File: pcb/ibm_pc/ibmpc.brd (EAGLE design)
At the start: 56 x 65 mm, 47 parts, among them IC1 STM32F072C8T6, SW1 324_SW, SW2 324_SW, U1 MAX3232

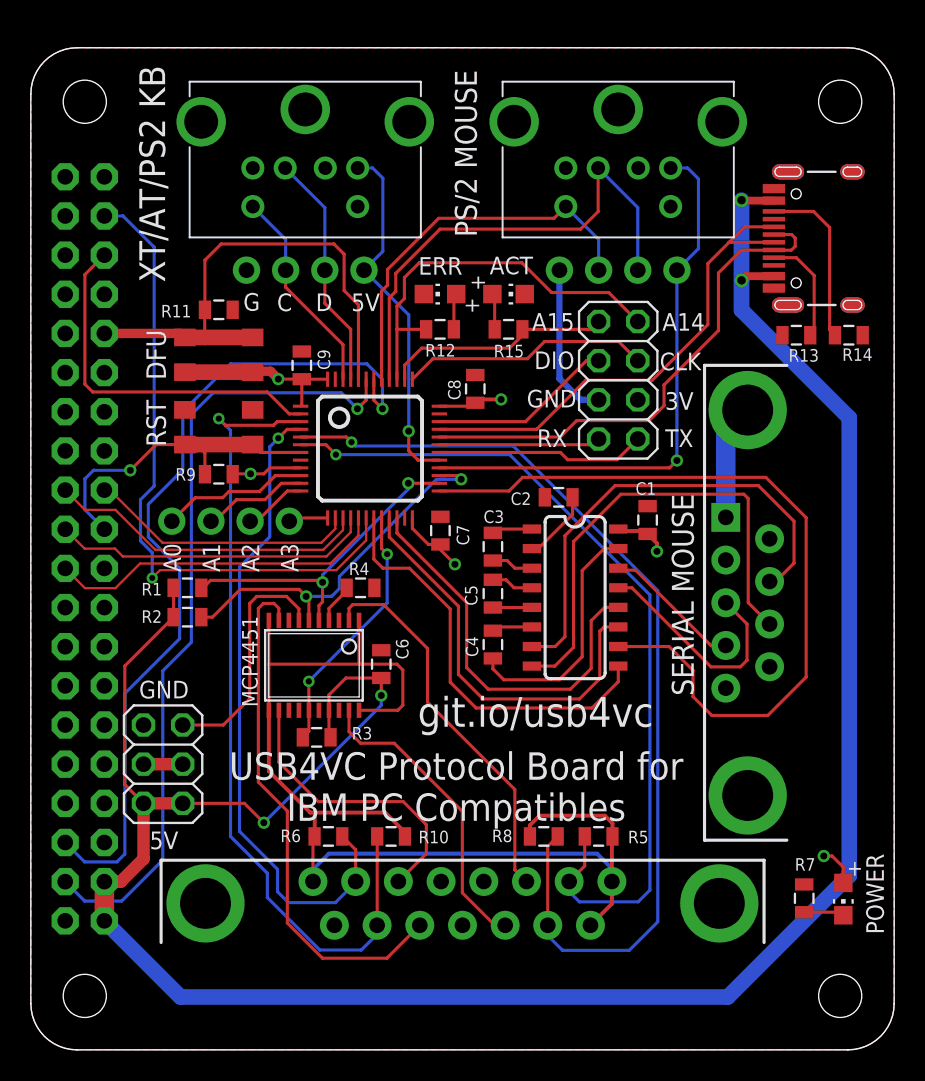
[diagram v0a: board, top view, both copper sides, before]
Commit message: added resistor to digipot
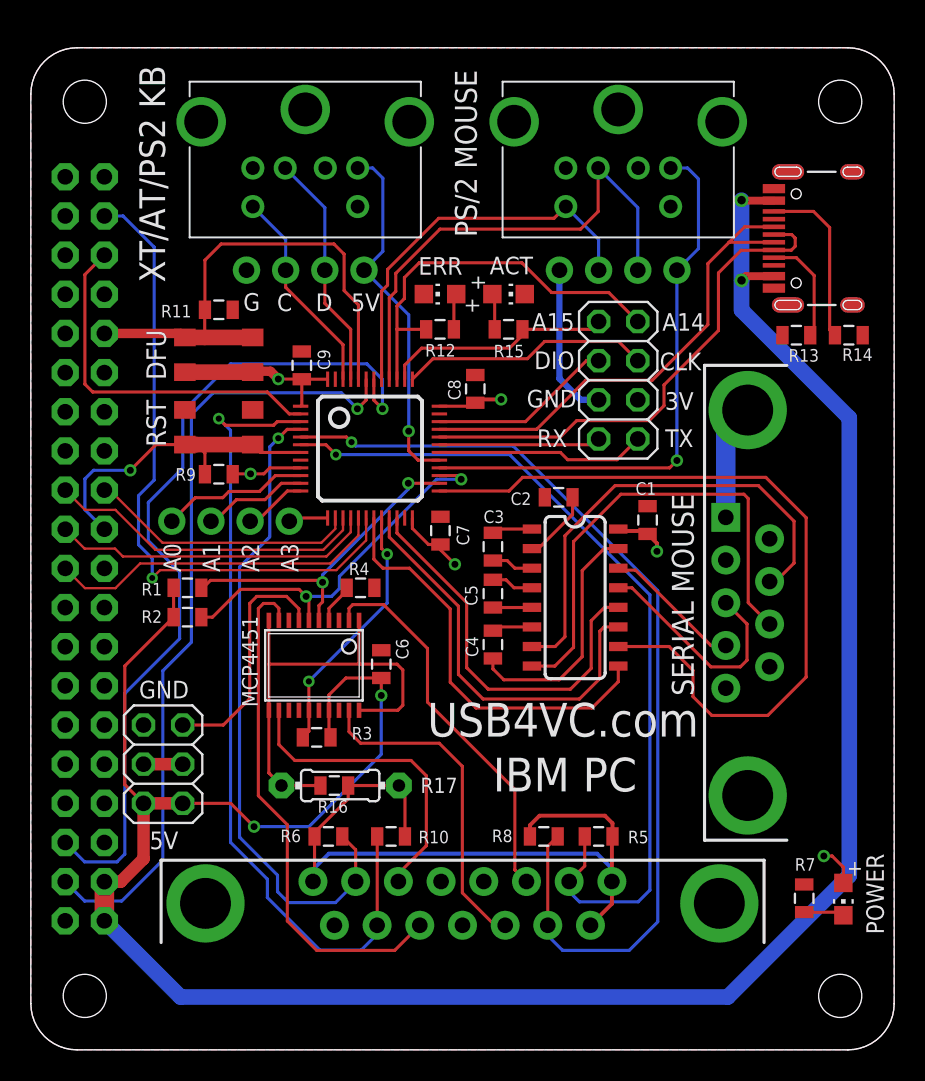
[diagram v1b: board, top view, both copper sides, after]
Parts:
- added R16: 100, SparkFun-Passives:0805
- added R17: (no value), adafruit:0204/7
- R12, R15, R7: value 2K -> 5.1K
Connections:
- new net N$17: R16.2, R17.1, U$5.1, U$5.10, U$5.11, U$5.20
- net +UB: now also R16.1, R17.2; no longer U$5.1, U$5.10, U$5.11, U$5.20
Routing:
- net N$17: track 0.00 -> 30.6 mm
- net +UB: track 77.6 -> 49.5 mm
- net +5V: track 157.3 -> 159.3 mm
- net X2_W2: track 19.8 -> 21.5 mm
- net Y1_W0: track 19.0 -> 20.2 mm
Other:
- board text added: "IBM PC"
- board text added: "USB4VC Protocol Card for IBM PC Compatible"
- board text added: "USB4VC.com"
- board text removed: "USB4VC Protocol Board for IBM PC Compatibles"
- board text removed: "git.io/usb4vc"

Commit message: updated IBM PC card
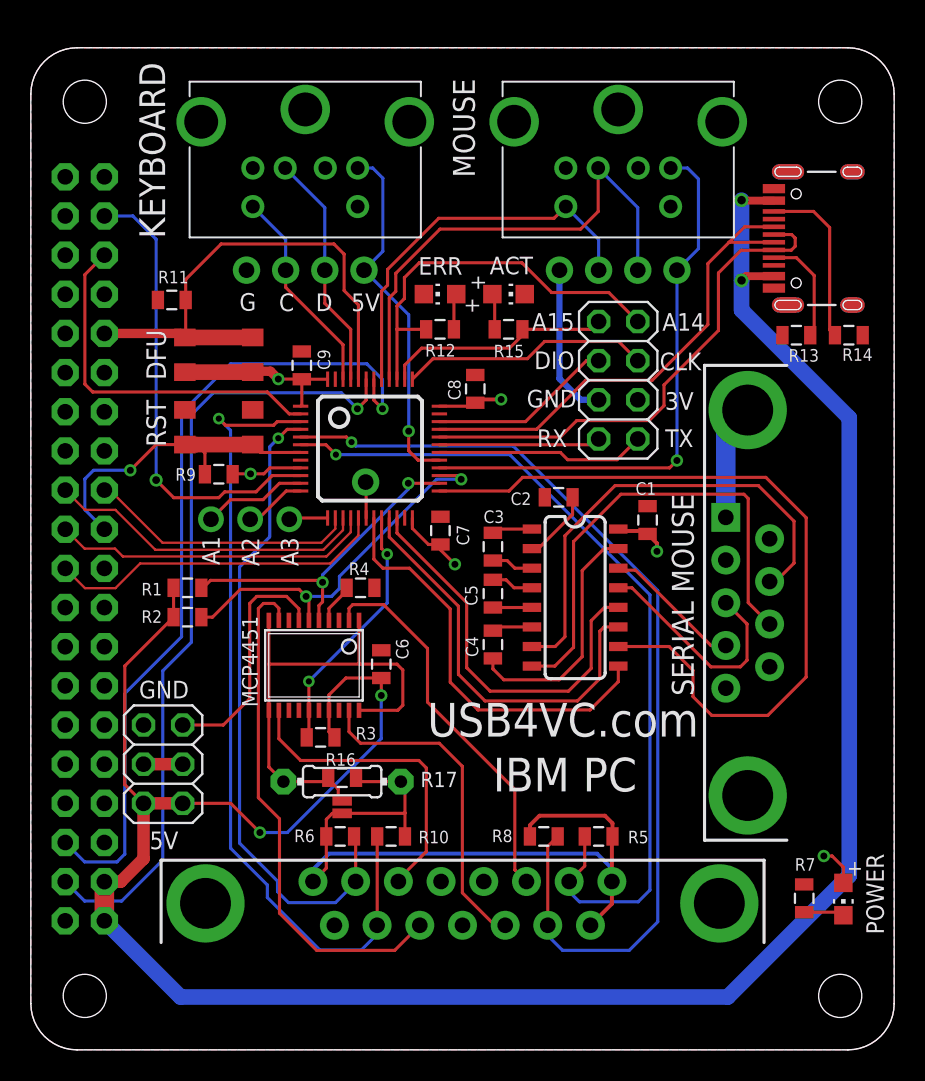
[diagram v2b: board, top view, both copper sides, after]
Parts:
- removed U$10: PINHD1X4, adafruit_changed:1X04-CLEANBIG
- added JP4: (no value), adafruit:1X03-CLEANBIG
- added JP5: JUMPER-SMT_2_NO_NO-SILK, SparkFun-Jumpers:SMT-JUMPER_2_NO_NO-SILK
- added JP6: (no value), adafruit:1X01-CLEANBIG
- moved R11 3.11 mm to (9.14, 48.6), turned to 0 degrees
- moved R6 0.76 mm to (20.1, 13.8)
- moved R16 0.72 mm to (20.2, 17.7)
- moved R17 0.28 mm to (20.2, 17.4)
- moved R3 0.25 mm to (18.8, 20.3)
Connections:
- removed net N$38: IC1.10, U$10.1
- new net N$30: IC1.18, JP6.1
- net +UB: now also JP5.2
- net N$17: now also JP5.1
- net N$3: now also IC1.10; no longer IC1.18
- net N$39: now also JP4.3; no longer U$10.2
- net N$40: now also JP4.2; no longer U$10.3
- net N$41: now also JP4.1; no longer U$10.4
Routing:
- net N$3: track 42.7 -> 30.0 mm
- net N$38: track 9.58 -> 0.00 mm
- net +UB: track 49.5 -> 51.9 mm
- net N$30: track 0.00 -> 2.34 mm
- net N$17: track 30.6 -> 32.7 mm
- net N$22: track 55.3 -> 53.6 mm
- net N$18: track 33.0 -> 33.5 mm
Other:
- board text added: "B0"
- board text added: "KEYBOARD"
- board text added: "MOUSE"
- board text added: "USB4VC Protocol Card for IBM PC Compatibles"
- board text removed: "A0"
- board text removed: "PS/2 MOUSE"
- board text removed: "USB4VC Protocol Card for IBM PC Compatible"
- board text removed: "XT/AT/PS2 KB"
